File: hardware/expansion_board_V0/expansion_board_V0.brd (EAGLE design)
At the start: 212 x 132 mm, 499 parts, among them CON1 ELEC, CON10 M5, CON11 M2, CON12 M4, CON13 M1, CON14 ESC0, CON15 CON10_2_2.54, CON16 CON10_2_2.54, CON17 ESC1, CON18 UART0, CON19 QEI1, CON2 SERVO, CON20 AN0, CON21 S0, CON22 IO0, CON23 AN1, CON24 S1, CON25 IO1, CON26 UART1, CON27 QEI0, CON28 AN2, CON29 S2, CON3 LIPO_MOT, CON30 IO2, CON31 TELEM, CON32 QEI3, CON33 AN3, CON34 S3, CON35 IO3, CON36 BALISE, CON37 AN4, CON38 S4, CON39 IO4, CON4 LIPO_MOT, CON40 SPI0, CON41 QEI2, CON42 AN5, CON43 S5, CON44 IO5, CON45 SPI1, CON46 AN6, CON47 S6, CON48 IO6, CON49 I2C0, CON5 LIPO_MOT, CON50 AN7, CON51 S7, CON52 IO7, CON53 I2C1, CON54 USB2, CON55 USB3, CON56 USBfpga, CON57 FPGA_GPIO0, CON58 FPGA_GPIO1, CON59 FPGA_LTC, CON6 LIPO_MOT, CON60 USB3, CON61 CON5_2.54S, CON62 CON5_2.54S, CON63 CON5_2.54S, CON64 CON5_2.54S, CON7 FPGApower, CON8 M0, CON9 M3, IC1 ADS1258, IC2 ADS1278, IC3 REF5030I, IC4 REF5025I, J1 NC, J10 0, J11 0, J12 0, J13 0, J14 0, J15 0, J16 0, J17 0, J18 0, J19 0, J2 nc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

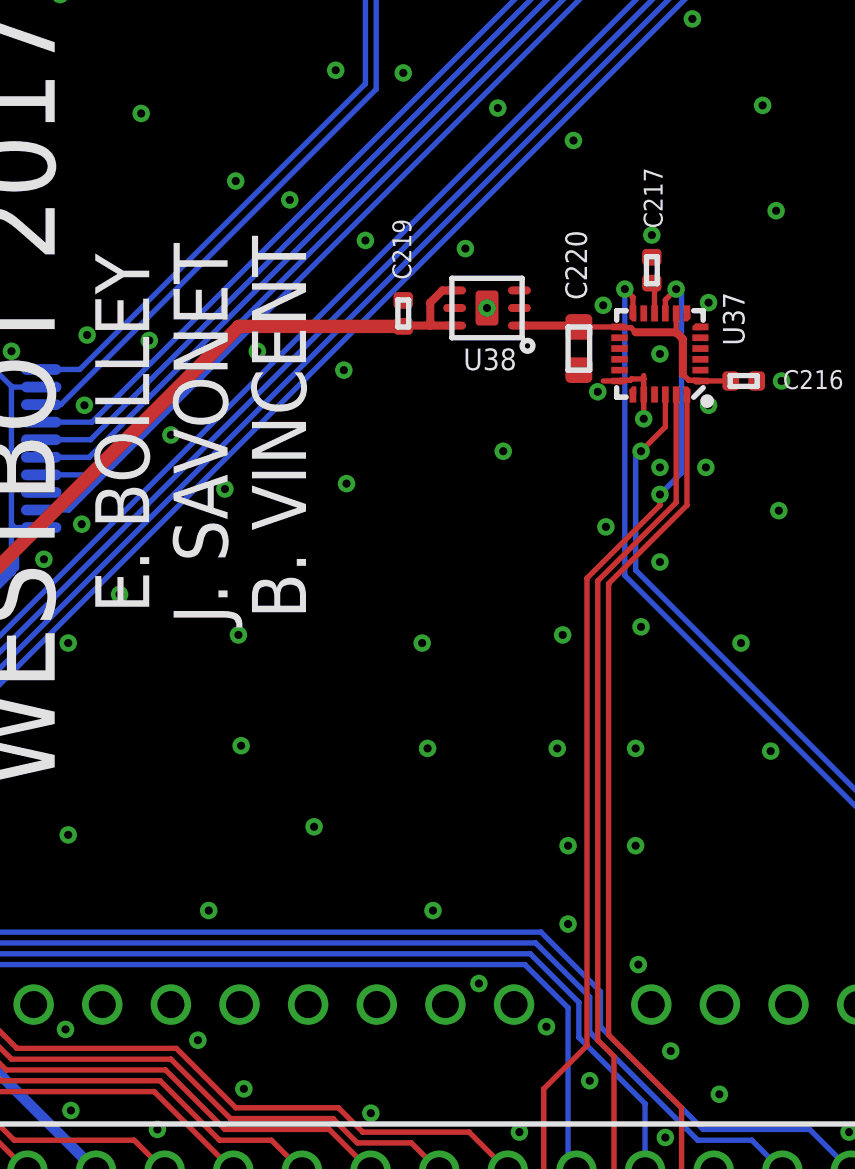
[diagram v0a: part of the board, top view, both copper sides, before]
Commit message: PCB envoyé chez eurocircuit
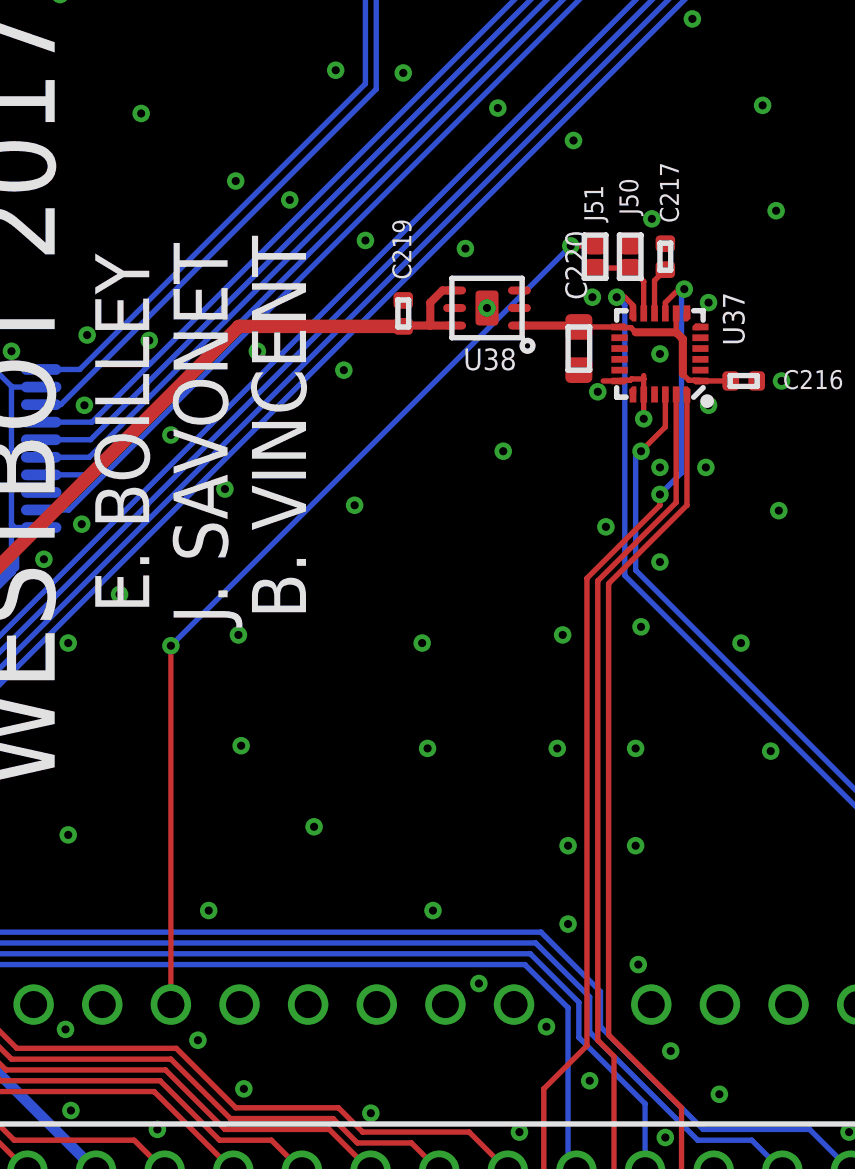
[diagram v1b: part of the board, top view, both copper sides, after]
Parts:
- added J50, J51: 0, iocene:JUMC1005X50N
- moved C217 0.71 mm to (-49.8, 3.60)
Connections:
- new net N$98: J50.P$2, J51.P$1, U37.11
- net GND: now also J50.P$1
- net IMU_FSYNC: now also J51.P$2, U29.RESET; no longer U37.11
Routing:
- net IMU_FSYNC: track 0.00 -> 35.1 mm, vias 0 -> 2
- net N$98: track 0.00 -> 3.19 mm
- net REGOUT1: track 1.16 -> 1.79 mm

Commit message: Derniere modif elec
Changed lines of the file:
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@@
 <wire x1="-88.22" y1="13.98" x2="-88.22" y2="19.98" width="0.2" layer="48"/>
 <wire x1="-88.22" y1="19.98" x2="-96.02" y2="19.98" width="0.2" layer="48"/>
-<wire x1="-179.8" y1="-120.8" x2="10.2" y2="-120.8" width="0.4064" layer="48"/>
-<wire x1="10.2" y1="-120.8" x2="10.2" y2="109.2" width="0.4064" layer="48"/>
-<wire x1="10.2" y1="109.2" x2="-179.8" y2="109.2" width="0.4064" layer="48"/>
-<wire x1="-179.8" y1="109.2" x2="-179.8" y2="-120.8" width="0.4064" layer="48"/>
 <wire x1="-3.001665625" y1="65" x2="-143.6" y2="65" width="0.2" layer="20"/>
 <wire x1="-143.6" y1="65" x2="-145" y2="63.6" width="0.2" layer="20" curve="90"/>
@@
 <wire x1="-217" y1="-72" x2="7" y2="-72" width="0.2" layer="47"/>
 <wire x1="7" y1="-72" x2="7" y2="72" width="0.2" layer="47"/>
+<hole x="-3.18" y="31.12" drill="3.2"/>
+<hole x="-3.18" y="-31.12" drill="3.2"/>
 </plain>
 <attributes>
@@
 <via x="-16.5" y="-39.4" extent="1-16" drill="0.3" diameter="0.65"/>
 <via x="-11.2" y="-40.8" extent="1-16" drill="0.3" diameter="0.65"/>
-<via x="-6.9" y="-31.1" extent="1-16" drill="0.3" diameter="0.65"/>
+<via x="-5.2" y="-32.8" extent="1-16" drill="0.3" diameter="0.65"/>
 <via x="-15.1" y="-28.6" extent="1-16" drill="0.3" diameter="0.65"/>
 <via x="-9.9" y="-28.6" extent="1-16" drill="0.3" diameter="0.65"/>
 <via x="-13.1" y="-24.9" extent="1-16" drill="0.3" diameter="0.65"/>
-<via x="-4.4" y="-26.9" extent="1-16" drill="0.3" diameter="0.65"/>
+<via x="-4.9" y="-29.1" extent="1-16" drill="0.3" diameter="0.65"/>
 <via x="-4.6" y="-18.7" extent="1-16" drill="0.3" diameter="0.65"/>
 <via x="-5.8" y="-13.1" extent="1-16" drill="0.3" diameter="0.65"/>
@@
 <via x="-16" y="23.1" extent="1-16" drill="0.3" diameter="0.65"/>
 <via x="-12.8" y="27.2" extent="1-16" drill="0.3" diameter="0.65"/>
-<via x="-8.6" y="31.4" extent="1-16" drill="0.3" diameter="0.65"/>
-<via x="-4.1" y="29.4" extent="1-16" drill="0.3" diameter="0.65"/>
+<via x="-5.6" y="32.5" extent="1-16" drill="0.3" diameter="0.65"/>
+<via x="-4.7" y="28.9" extent="1-16" drill="0.3" diameter="0.65"/>
 <via x="-8.8" y="36.7" extent="1-16" drill="0.3" diameter="0.65"/>
 <via x="-20.6" y="36" extent="1-16" drill="0.3" diameter="0.65"/>
@@
 <wire x1="-1" y1="42" x2="-2.3" y2="38.4" width="0" layer="19" extent="1-1"/>
 <wire x1="-4.8" y1="41.6" x2="-1" y2="42" width="0" layer="19" extent="1-1"/>
-<wire x1="-4.1" y1="29.4" x2="-1" y2="32" width="0" layer="19" extent="1-1"/>
-<wire x1="-1" y1="27" x2="-4.1" y2="29.4" width="0" layer="19" extent="1-1"/>
+<wire x1="-4.7" y1="28.9" x2="-1" y2="32" width="0" layer="19" extent="1-1"/>
+<wire x1="-1" y1="27" x2="-4.7" y2="28.9" width="0" layer="19" extent="1-1"/>
 <wire x1="-4.4" y1="10.9" x2="-8.48" y2="8.57" width="0" layer="19" extent="1-1"/>
 <wire x1="-1" y1="12" x2="-4.4" y2="10.9" width="0" layer="19" extent="1-1"/>
@@
 <wire x1="-1" y1="-13" x2="-5.8" y2="-13.1" width="0" layer="19" extent="1-1"/>
 <wire x1="-66.7" y1="-20.6" x2="-67.1" y2="-25.4" width="0" layer="19" extent="1-1"/>
-<wire x1="-8.6" y1="31.4" x2="-8.48" y2="26.57" width="0" layer="19" extent="1-1"/>
+<wire x1="-5.6" y1="32.5" x2="-8.48" y2="26.57" width="0" layer="19" extent="1-1"/>
 <wire x1="-68" y1="64" x2="-71.12" y2="60.325" width="0" layer="19" extent="1-1"/>
 <wire x1="-209" y1="2" x2="-204.3" y2="0.8" width="0" layer="19" extent="1-1"/>
@@
 <wire x1="-7.2" y1="51.2" x2="-4.1" y2="55" width="0" layer="19" extent="1-1"/>
 <wire x1="-9.9" y1="-28.6" x2="-13.1" y2="-24.9" width="0" layer="19" extent="1-1"/>
-<wire x1="-6.9" y1="-31.1" x2="-9.9" y2="-28.6" width="0" layer="19" extent="1-1"/>
-<wire x1="-4.4" y1="-26.9" x2="-6.9" y2="-31.1" width="0" layer="19" extent="1-1"/>
-<wire x1="-1" y1="-28" x2="-4.4" y2="-26.9" width="0" layer="19" extent="1-1"/>
+<wire x1="-5.2" y1="-32.8" x2="-9.9" y2="-28.6" width="0" layer="19" extent="1-1"/>
+<wire x1="-4.9" y1="-29.1" x2="-5.2" y2="-32.8" width="0" layer="19" extent="1-1"/>
+<wire x1="-1" y1="-28" x2="-4.9" y2="-29.1" width="0" layer="19" extent="1-1"/>
 <wire x1="-44.7" y1="58.9" x2="-49.6" y2="58.9" width="0" layer="19" extent="1-1"/>
 <wire x1="-40.3" y1="60.6" x2="-44.7" y2="58.9" width="0" layer="19" extent="1-1"/>

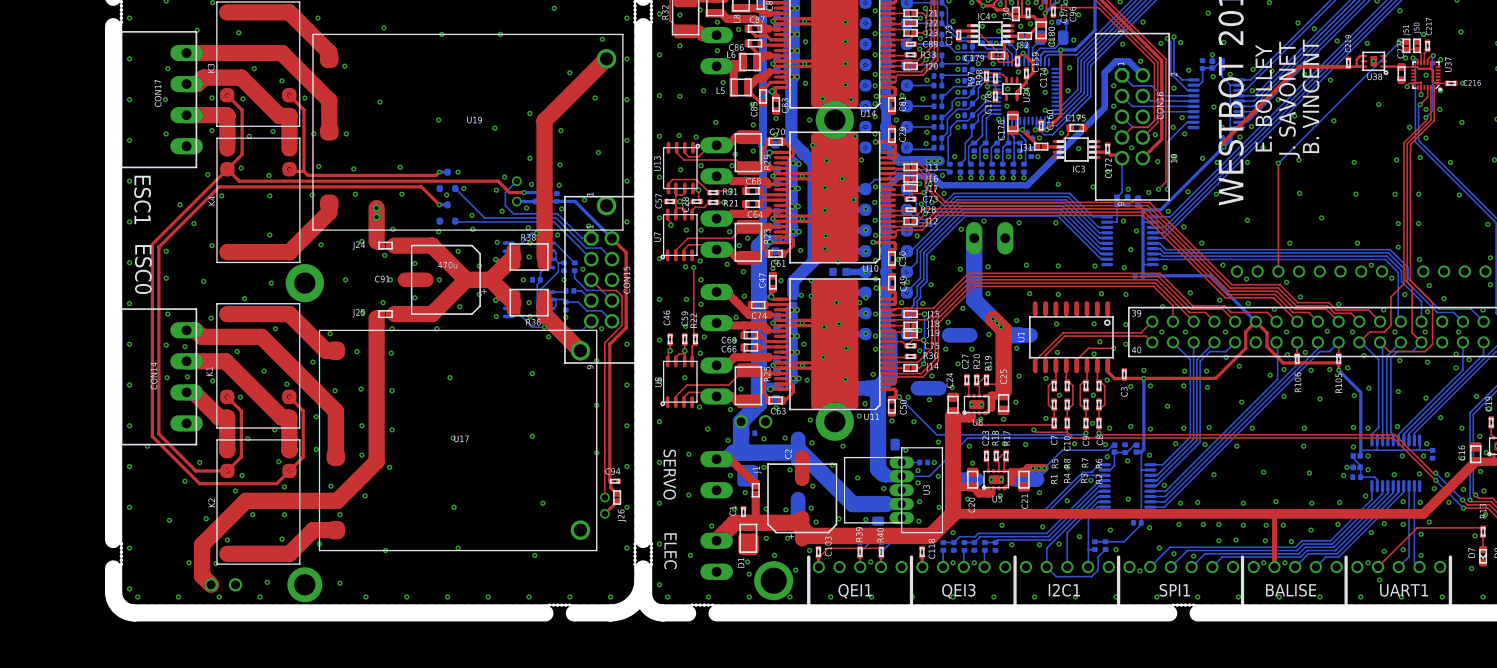
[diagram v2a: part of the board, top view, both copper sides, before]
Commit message: Update schematics with new library
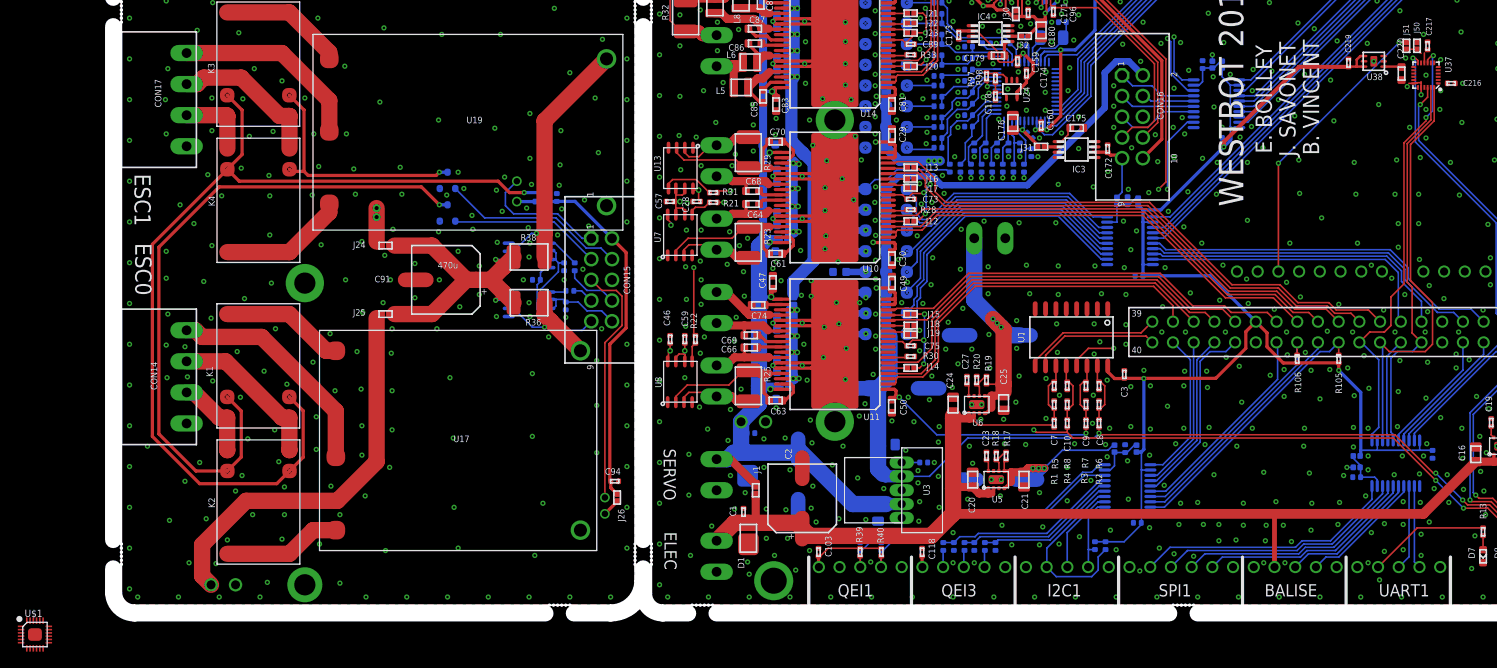
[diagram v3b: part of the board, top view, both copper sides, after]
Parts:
- added U$1: MPU-9250, invensense:LEAD-QFN24
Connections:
- new net N$107: C217.2, U$1.10
- new net N$141: U37.1, U37.13, U37.8
- net GND: now also U$1.18, U$1.20, U$1.25
- net IMU_DRDY: now also U$1.12
- net IMU_SS: now also U$1.22
- net MISO1: now also U$1.9
- net MOSI1: now also U$1.24
- net N$74: now also U$1.1, U$1.13, U$1.8; no longer U37.1, U37.13, U37.8
- net N$98: now also U$1.11; no longer U37.11
- net REGOUT1: no longer C217.2
- net SCLK1: now also U$1.23
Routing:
- net N$74: track 10.1 -> 2.22 mm
- net N$98: track 3.19 -> 2.01 mm
- net REGOUT1: track 1.79 -> 1.22 mm

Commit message: IMU footprint ok Elec posté sur Eurocircuit
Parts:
- removed U$1: MPU-9250, invensense:LEAD-QFN24
- moved C217 0.10 mm to (-49.8, 3.70)
- moved J50 0.10 mm to (-51.1, 3.70)
- moved J51 0.10 mm to (-52.4, 3.70)
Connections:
- removed net N$107: C217.2, U$1.10
- removed net N$141: U37.1, U37.13, U37.8
- net GND: now also U37.14, U37.15, U37.16, U37.17, U37.2, U37.3, U37.4, U37.5, U37.6, U37.PAD; no longer U$1.18, U$1.20, U$1.25
- net IMU_DRDY: no longer U$1.12
- net IMU_SS: no longer U$1.22
- net MISO1: no longer U$1.9
- net MOSI1: no longer U$1.24
- net N$74: now also U37.1, U37.13, U37.8; no longer U$1.1, U$1.13, U$1.8
- net N$98: now also U37.11; no longer U$1.11
- net REGOUT1: now also C217.2
- net SCLK1: no longer U$1.23
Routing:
- net N$74: track 2.22 -> 23.7 mm
- net GND: track 244.6 -> 242.9 mm
- net MISO1: track 54.8 -> 56.2 mm
- net N$98: track 2.01 -> 3.24 mm
- net REGOUT1: track 1.22 -> 1.84 mm
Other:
- outline, holes or cut-outs redrawn
- board text added: "LEDA"
- board text added: "LEDB"
- board text added: "servo"

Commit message: Ajout de commentaires bug carte électronique sur le schéma
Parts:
- C114, C117, C134, C137: value 100n -> nc
- C168, C169: value 22n -> 8p
- C19: value nc -> 22n
- C23: value nc -> 1n
- R100, R101, R102, R103, R104, R105, R106, R99: value 10k -> 50k
- R44, R49, R56, R64, R69, R77, R82, R87: value 10k -> 20k
- R54, R60, R80, R85: value 10k -> 560
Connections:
- net M4_CS renamed M5_CS

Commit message: Add datasheet capteur couleur
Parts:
- C114: value nc -> 100n
- R42, R47, R67, R75: value 10k -> 1k
- R54: value 560 -> 1k
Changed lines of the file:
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@@
 <layers>
 <layer number="1" name="Top" color="4" fill="1" visible="yes" active="yes"/>
-<layer number="2" name="Route2" color="13" fill="3" visible="no" active="yes"/>
+<layer number="2" name="Route2" color="13" fill="3" visible="yes" active="yes"/>
 <layer number="3" name="Route3" color="4" fill="3" visible="no" active="no"/>
 <layer number="4" name="Route4" color="1" fill="4" visible="no" active="no"/>
@@
 <attribute name="VALUE" x="-110.655" y="16.24" size="0.8" layer="28" font="vector" rot="MR180"/>
 </element>
-<element name="C114" library="iocene" package="CAPC1005X55N" value="nc" x="-109.855" y="17.78" smashed="yes" rot="MR180">
+<element name="C114" library="iocene" package="CAPC1005X55N" value="100n" x="-109.855" y="17.78" smashed="yes" rot="MR180">
 <attribute name="NAME" x="-108.855" y="18.18" size="0.8" layer="26" font="vector" rot="MR180"/>
 <attribute name="VALUE" x="-110.655" y="18.78" size="0.8" layer="28" font="vector" rot="MR180"/>
@@
 <attribute name="VALUE" x="-23.9" y="13.1" size="0.8" layer="27" font="vector"/>
 </element>
-<element name="R42" library="iocene" package="RESC1005X40N" value="10k" x="-109.855" y="13.97" smashed="yes" rot="MR180">
+<element name="R42" library="iocene" package="RESC1005X40N" value="1k" x="-109.855" y="13.97" smashed="yes" rot="MR180">
 <attribute name="NAME" x="-108.855" y="13.87" size="0.8" layer="26" font="vector" rot="MR180"/>
 <attribute name="VALUE" x="-110.655" y="14.97" size="0.8" layer="28" font="vector" rot="MR180"/>
 </element>
-<element name="R47" library="iocene" package="RESC1005X40N" value="10k" x="-109.855" y="16.51" smashed="yes" rot="MR180">
+<element name="R47" library="iocene" package="RESC1005X40N" value="1k" x="-109.855" y="16.51" smashed="yes" rot="MR180">
 <attribute name="NAME" x="-108.855" y="16.91" size="0.8" layer="26" font="vector" rot="MR180"/>
 <attribute name="VALUE" x="-110.655" y="17.51" size="0.8" layer="28" font="vector" rot="MR180"/>
 </element>
-<element name="R54" library="iocene" package="RESC1005X40N" value="560" x="-109.855" y="19.05" smashed="yes" rot="MR180">
+<element name="R54" library="iocene" package="RESC1005X40N" value="1k" x="-109.855" y="19.05" smashed="yes" rot="MR180">
 <attribute name="NAME" x="-108.855" y="19.45" size="0.8" layer="26" font="vector" rot="MR180"/>
 <attribute name="VALUE" x="-110.655" y="20.05" size="0.8" layer="28" font="vector" rot="MR180"/>
@@
 <attribute name="VALUE" x="-110.655" y="22.59" size="0.8" layer="28" font="vector" rot="MR180"/>
 </element>
-<element name="R67" library="iocene" package="RESC1005X40N" value="10k" x="-109.855" y="24.13" smashed="yes" rot="MR180">
+<element name="R67" library="iocene" package="RESC1005X40N" value="1k" x="-109.855" y="24.13" smashed="yes" rot="MR180">
 <attribute name="NAME" x="-108.855" y="24.63" size="0.8" layer="26" font="vector" rot="MR180"/>
 <attribute name="VALUE" x="-110.655" y="25.13" size="0.8" layer="28" font="vector" rot="MR180"/>
@@
 <attribute name="VALUE" x="-120.42" y="-27.87" size="0.8" layer="28" font="vector" rot="MR0"/>
 </element>
-<element name="R75" library="iocene" package="RESC1005X40N" value="10k" x="-109.855" y="26.67" smashed="yes" rot="MR180">
+<element name="R75" library="iocene" package="RESC1005X40N" value="1k" x="-109.855" y="26.67" smashed="yes" rot="MR180">
 <attribute name="NAME" x="-108.855" y="27.07" size="0.8" layer="26" font="vector" rot="MR180"/>
 <attribute name="VALUE" x="-110.655" y="27.67" size="0.8" layer="28" font="vector" rot="MR180"/>

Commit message: elec ok
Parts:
- C108: value 100n -> NC
- C117: value nc -> 100n
- C119, C120, C121, C126, C127, C128: value 1n -> 100p
- C56, C58, C71, C76, C90, C95, C96: value 1n -> 100n
- R1, R2, R3: value 100k -> 3.3k
- R21, R22, R27, R31, R34, R35, R37: value 10k -> 100
- R4: value 100k -> 33k
- R47: value 1k -> 33
- R5, R6, R7: value 5k -> 1k
- R58, R61, R62, R71, R72, R73: value 1k -> 100
- R60: value 560 -> 1k
- R8: value 5k -> 3.3k
- R80, R85: value 560 -> 33
